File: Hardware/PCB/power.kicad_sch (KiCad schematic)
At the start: 8 parts, among them J4 Power Input, U5 R-78E5.0-1.0, U6 AP7361C-33E

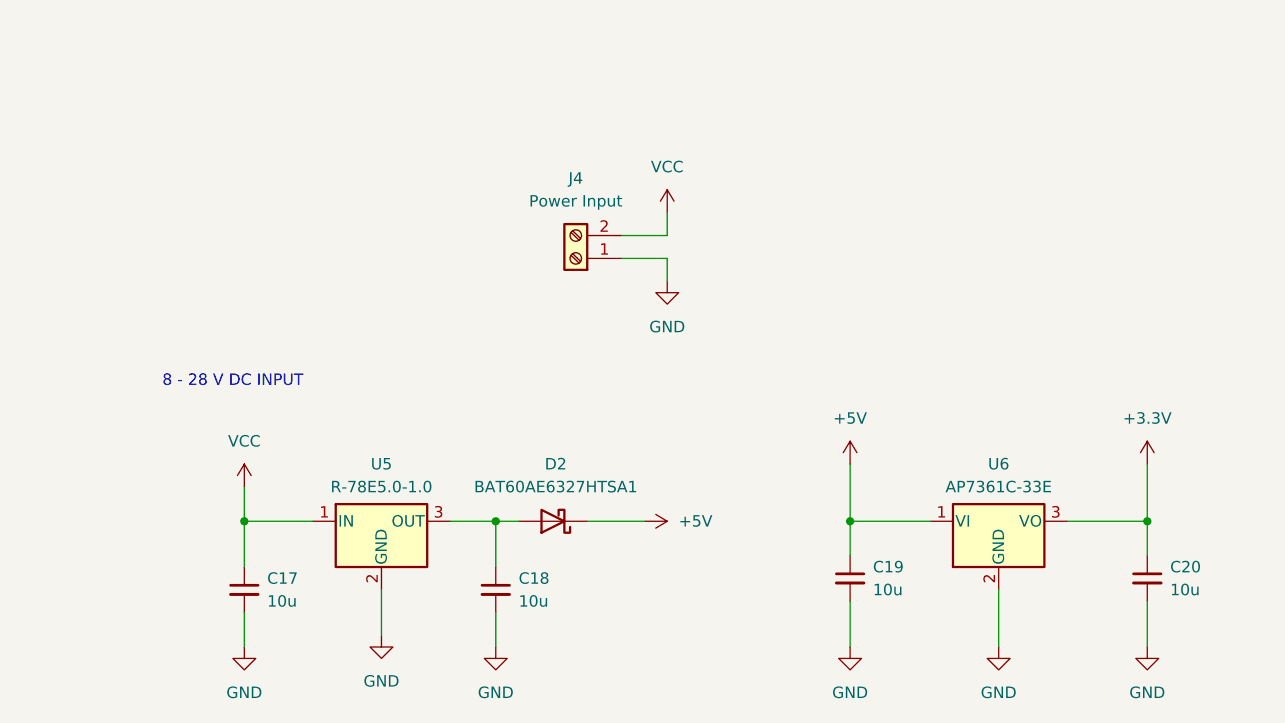
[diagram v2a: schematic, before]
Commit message: switched to making buck converter to save costs and space, and to allow for LDO after 5.5V for better stability
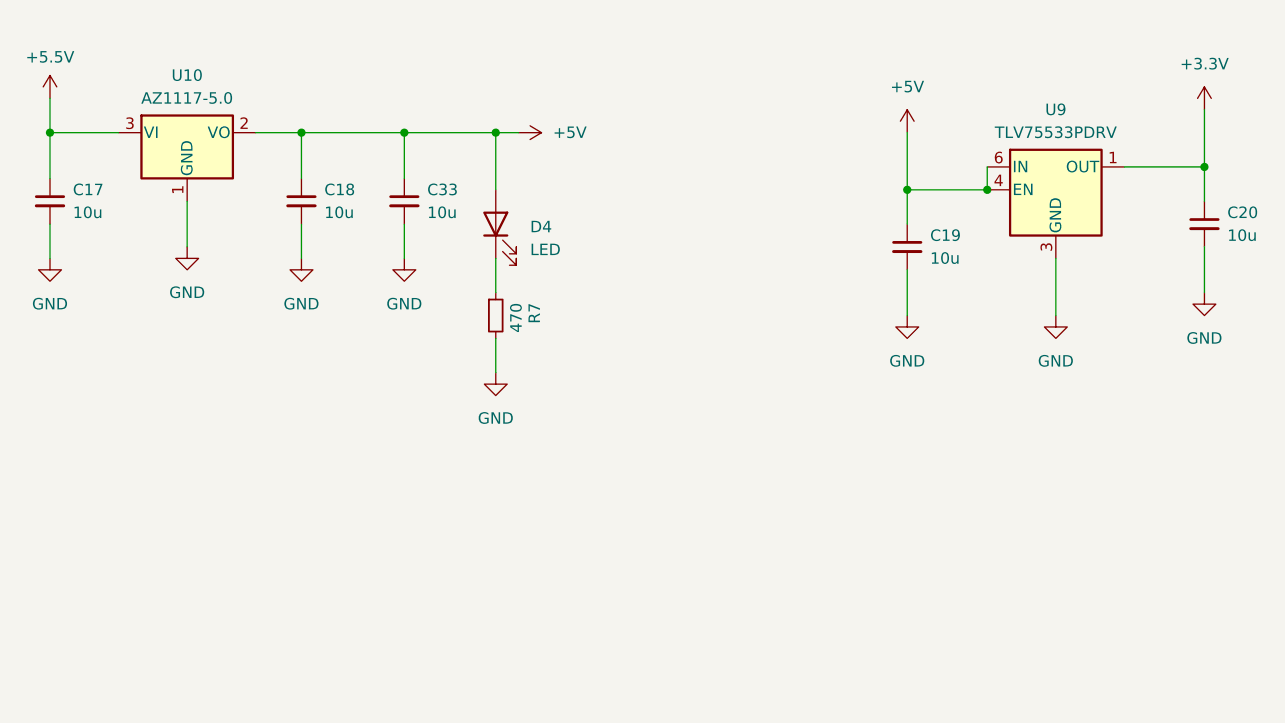
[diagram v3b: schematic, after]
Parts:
- removed D2: BAT60AE6327HTSA1, Diode_SMD:D_SOD-323_HandSoldering, symbol Device:D_Schottky
- removed J4: Power Input, Vendor_Footprints:PHOENIX_1984963, symbol Connector:Screw_Terminal_01x02
- removed U5: R-78E5.0-1.0, Converter_DCDC:Converter_DCDC_RECOM_R-78E-0.5_THT, symbol Regulator_Switching:R-78E5.0-1.0
- removed U6: AP7361C-33E, Package_TO_SOT_SMD:SOT-223-3_TabPin2, symbol Regulator_Linear:AP7361C-33E
- added C33: 10u, Capacitor_SMD:C_0805_2012Metric_Pad1.18x1.45mm_HandSolder, symbol Device:C_Small
- added D4: LED, LED_SMD:LED_0603_1608Metric_Pad1.05x0.95mm_HandSolder, symbol Device:LED
- added R7: 470, Resistor_SMD:R_0603_1608Metric_Pad0.98x0.95mm_HandSolder, symbol Device:R_Small
- added U10: AZ1117-5.0, Package_TO_SOT_SMD:SOT-223-3_TabPin2, symbol Regulator_Linear:AZ1117-5.0
- added U9: TLV75533PDRV, Package_SON:WSON-6-1EP_2x2mm_P0.65mm_EP1x1.6mm, symbol Regulator_Linear:TLV75533PDRV
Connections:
- net +3.3V: now also U9.1 (OUT)
- net +5V: now also C18.1, C33.1, D4.2 (A), U10.2 (VO), U9.4 (EN), U9.6 (IN)
- net GND: now also C33.2, R7.2, U10.1 (GND), U9.3 (GND), U9.7 (GND)
- net VCC renamed +5.5V
- net +5.5V: now also U10.3 (VI)
- new net: D4.1 (K), R7.1
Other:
- note removed: "8 - 28 V DC INPUT"
- moved on the sheet: C17, C18, C19, C20

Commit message: swapped to be better precision resistors for feedback on buck and votlage reference for ADCs
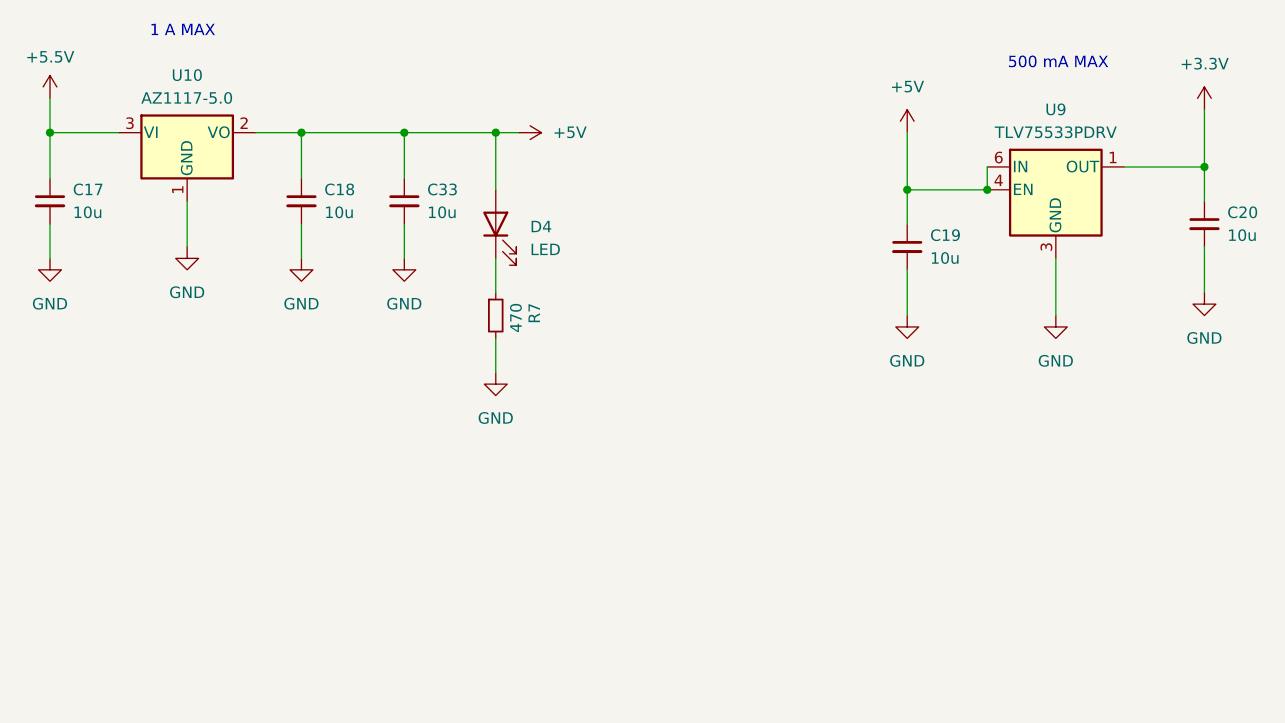
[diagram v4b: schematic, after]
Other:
- note added: "1 A MAX"
- note added: "500 mA MAX"
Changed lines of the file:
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@@
+		)
+	)
+	(text "500 mA MAX"
+		(exclude_from_sim no)
+		(at 176.784 33.02 0)
+		(effects
+			(font
+				(size 1.27 1.27)
+			)
+		)
+	)
+	(text "1 A MAX"
+		(exclude_from_sim no)
+		(at 79.502 29.464 0)
+		(effects
+			(font
+				(size 1.27 1.27)
+			)
 		)
 	)
